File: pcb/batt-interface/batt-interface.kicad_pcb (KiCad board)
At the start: 2 copper layers, 33.5 x 14.4 mm, 12 parts, among them IC1 MCP73831T-2ACI_OT, J1 UJC-H-G-SMT-2-P6-TR, J2 Battery, J3 Load

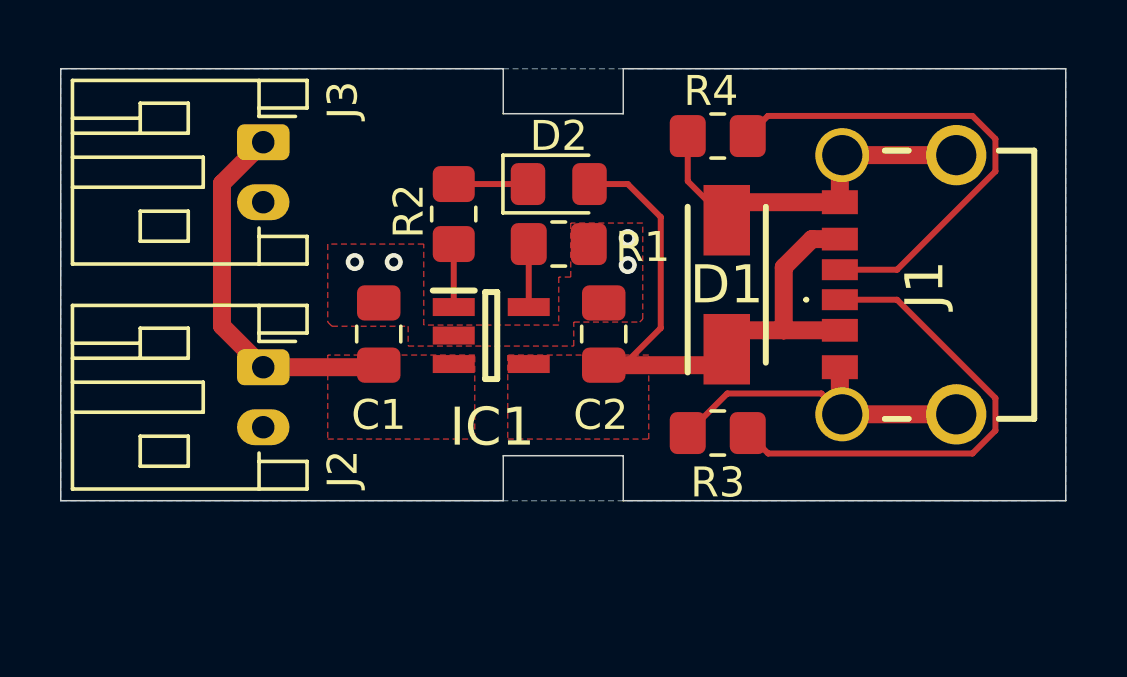
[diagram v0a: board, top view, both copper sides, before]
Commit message: Check in changes to the PCB files. Also checkin main.cpp change to clarify LED colors of status lights
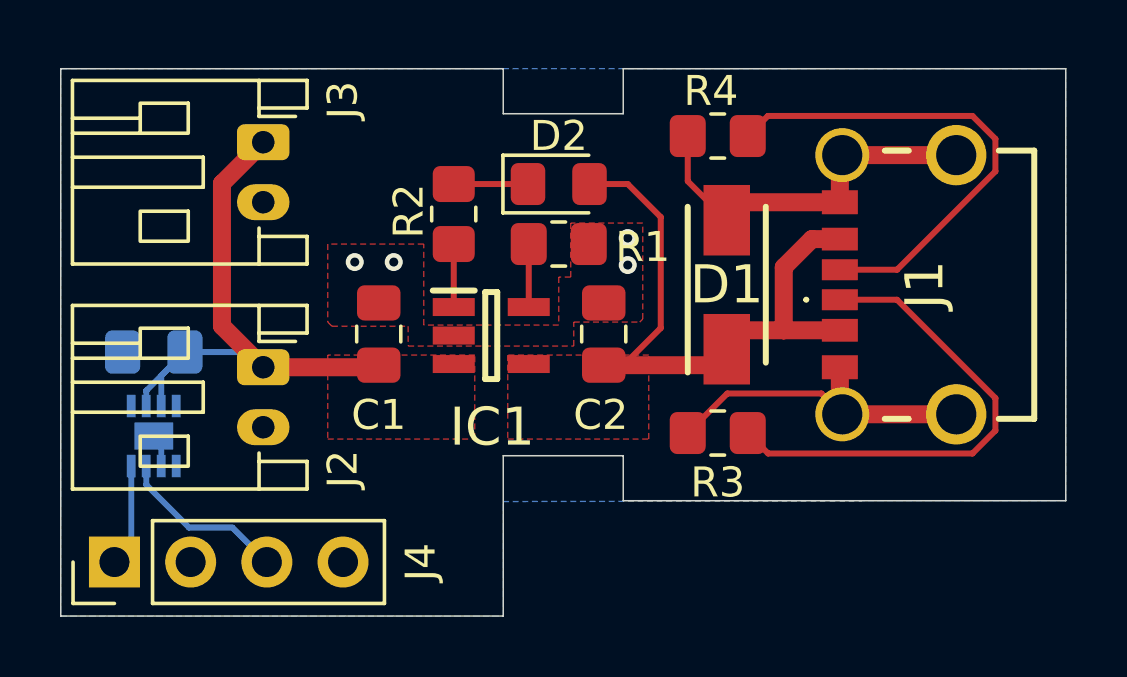
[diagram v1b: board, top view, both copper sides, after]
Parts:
- added C3: .1uF, Capacitor_SMD:C_0805_2012Metric_Pad1.18x1.45mm_HandSolder, B.Cu at (111.5, 76.6)
- added IC2: MAX17048G+T10, Garth:SON50P200X200X80-9N-D, B.Cu at (111.5, 79.4)
- added J4: i2c, Connector_PinHeader_2.54mm:PinHeader_1x04_P2.54mm_Vertical, F.Cu at (110.2, 83.6)
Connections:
- J1 pad A5: unconnected-(J1-CC1-PadA5) -> Net-(J1-CC1)
- J1 pad B5: unconnected-(J1-CC2-PadB5) -> Net-(J1-CC2)
- R3 pad 1: unconnected-(J1-CC1-PadA5) -> Net-(J1-CC1)
- R4 pad 1: unconnected-(J1-CC2-PadB5) -> Net-(J1-CC2)
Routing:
- net unconnected-(J1-CC1-PadA5): track 16.5 -> 0.00 mm
- net Net-(J1-CC1): track 0.00 -> 16.5 mm
- net unconnected-(J1-CC2-PadB5): track 16.5 -> 0.00 mm
- net Net-(J1-CC2): track 0.00 -> 16.5 mm
- net +BATT: track 12.5 -> 19.8 mm
- net /SCL: track 0.00 -> 5.71 mm
- net /SDA: track 0.00 -> 3.43 mm
- net GND: track 25.0 -> 26.1 mm
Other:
- board size 33.5 x 14.4 mm -> 33.5 x 18.2 mm
- board text added: "2026-01-03 v1.2"
- board text removed: "2026-01-03 v1.1"
